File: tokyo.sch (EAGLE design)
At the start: 49 parts, among them J1 254-2X5F, J2 254-2X5M, P1 9774050151, P2 9774050151, P3 9774050151, P4 9774050151, Q1 STD6N95K5, T1 750313823, U1 UCC28710, X1 508-1X3B

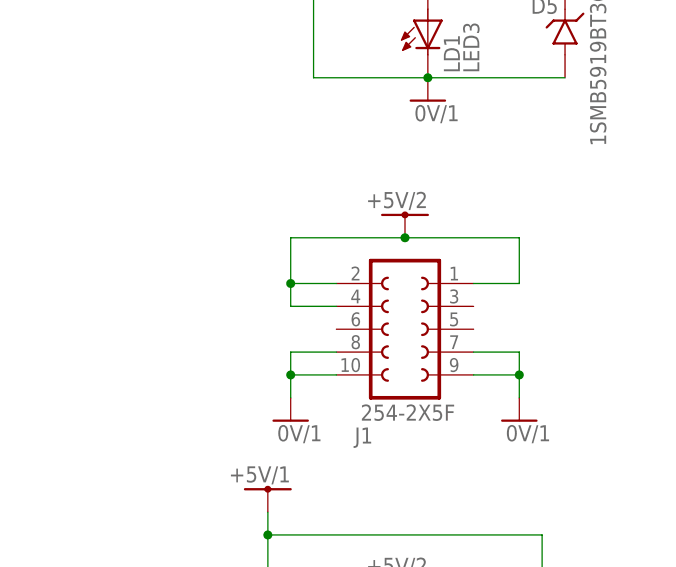
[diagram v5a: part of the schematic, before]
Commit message: Corrected +5V/2 routing.
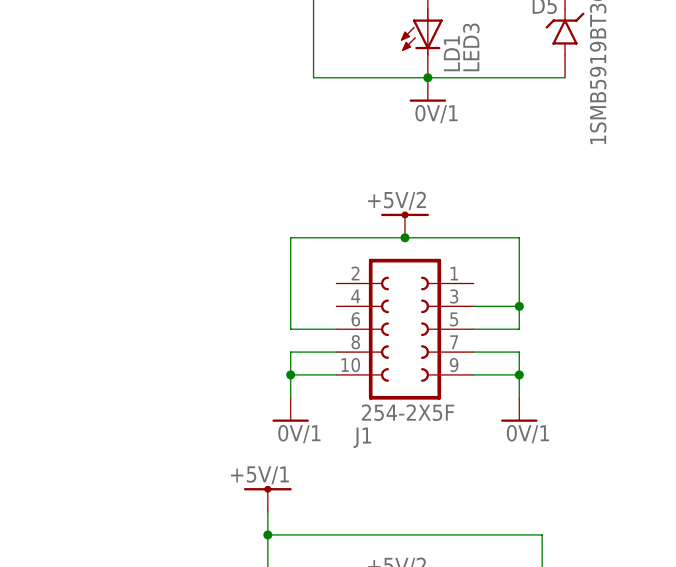
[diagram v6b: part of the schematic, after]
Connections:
- net +5V/2: now also J1.3, J1.5, J1.6; no longer J1.1, J1.2, J1.4
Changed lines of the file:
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@@
 <?xml version="1.0" encoding="utf-8"?>
 <!DOCTYPE eagle SYSTEM "eagle.dtd">
-<eagle version="7.3.0">
+<eagle version="7.6.0">
 <drawing>
 <settings>
@@
 <net name="+5V/2" class="0">
 <segment>
-<pinref part="J1" gate="G$1" pin="1"/>
-<wire x1="358.14" y1="165.1" x2="363.22" y2="165.1" width="0.1524" layer="91"/>
-<wire x1="363.22" y1="165.1" x2="363.22" y2="170.18" width="0.1524" layer="91"/>
-<pinref part="J1" gate="G$1" pin="4"/>
-<wire x1="342.9" y1="162.56" x2="337.82" y2="162.56" width="0.1524" layer="91"/>
-<wire x1="337.82" y1="162.56" x2="337.82" y2="165.1" width="0.1524" layer="91"/>
-<pinref part="J1" gate="G$1" pin="2"/>
-<wire x1="342.9" y1="165.1" x2="337.82" y2="165.1" width="0.1524" layer="91"/>
-<junction x="337.82" y="165.1"/>
 <wire x1="363.22" y1="170.18" x2="350.52" y2="170.18" width="0.1524" layer="91"/>
 <wire x1="350.52" y1="170.18" x2="337.82" y2="170.18" width="0.1524" layer="91"/>
-<wire x1="337.82" y1="170.18" x2="337.82" y2="165.1" width="0.1524" layer="91"/>
 <pinref part="U$12" gate="G$1" pin="+5V/2"/>
 <junction x="350.52" y="170.18"/>
-</segment>
-<segment>
+<pinref part="J1" gate="G$1" pin="5"/>
+<wire x1="358.14" y1="160.02" x2="363.22" y2="160.02" width="0.1524" layer="91"/>
+<wire x1="363.22" y1="160.02" x2="363.22" y2="162.56" width="0.1524" layer="91"/>
+<wire x1="363.22" y1="162.56" x2="363.22" y2="170.18" width="0.1524" layer="91"/>
+<wire x1="337.82" y1="170.18" x2="337.82" y2="160.02" width="0.1524" layer="91"/>
+<pinref part="J1" gate="G$1" pin="6"/>
+<wire x1="337.82" y1="160.02" x2="342.9" y2="160.02" width="0.1524" layer="91"/>
+<pinref part="J1" gate="G$1" pin="3"/>
+<wire x1="358.14" y1="162.56" x2="363.22" y2="162.56" width="0.1524" layer="91"/>
+<junction x="363.22" y="162.56"/>
+</segment>
+<segment>
